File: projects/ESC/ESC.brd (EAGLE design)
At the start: 139.7 x 38.1 mm, 93 parts, among them J1 1755529, J2 1755529, J3 1755529, J4 1755529, U1 STM32F405RGT6, U10 CSD88584Q5DCT, U11 CSD88584Q5DCT, U12 CSD88584Q5DCT, U13 CSD88584Q5DCT, U14 SN74CBTLV3257PWR, U2 CSD88584Q5DCT, U3 CSD88584Q5DCT, U4 CSD88584Q5DCT, U5 CSD88584Q5DCT, U6 CSD88584Q5DCT, U7 CSD88584Q5DCT, U8 CSD88584Q5DCT, U9 CSD88584Q5DCT, Y1 ECS-80-S-4X

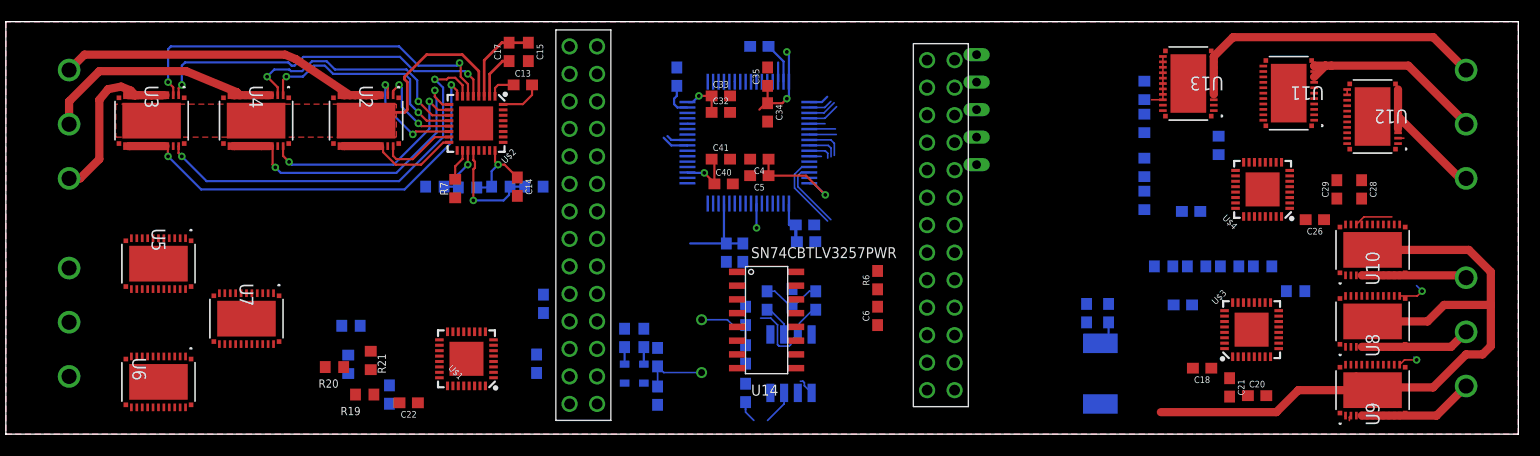
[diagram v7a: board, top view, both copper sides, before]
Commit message: All 4 drive ckts complete
Added and implemented design block across all 4 motors.
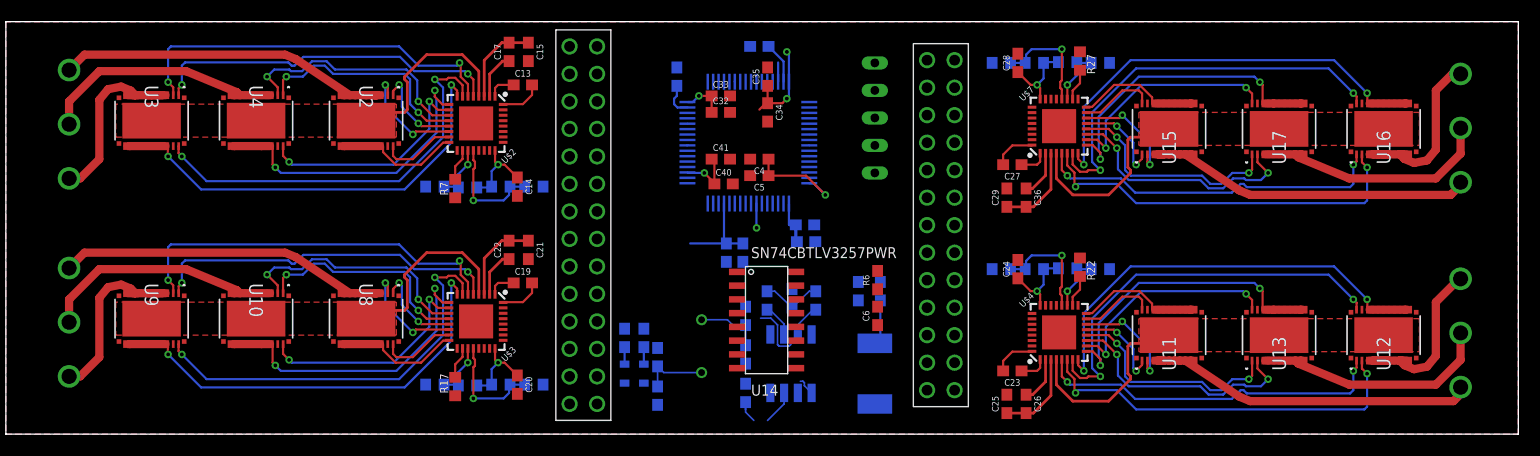
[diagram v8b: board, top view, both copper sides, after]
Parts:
- removed C18: 47nF, SparkFun-Capacitors:0603
- removed R13: 47k, rcl:R0603
- removed R14, R15, R16: (no value), rcl:R0603
- removed U$1: DRV8320H, VESC_SHIT:QFN-32-5X5MM
- removed U5, U6, U7: CSD88584Q5DCT, VESC_SHIT:DMM0022A
- added C36: 1.0uF, SparkFun-Capacitors:0603
- added R30, R31, R32, R33: (no value), rcl:R0603
- added U$7: DRV8320H, VESC_SHIT:QFN-32-5X5MM
- added U15, U16, U17: CSD88584Q5DCT, VESC_SHIT:DMM0022A
- C19, C23, C27: value 1.0uF -> 47nF
- C20, C24, C28: value 0.1uF -> 1.0uF
- C21, C25, C29: value 1.0uF -> 0.1uF
- C22, C26: value 47nF -> 1.0uF
- R17, R22, R27: value (none) -> 47k
- R18, R23: value 47k -> (none)
- moved U9 113.0 mm to (13.5, 10.7), turned to 270 degrees
- moved U10 103.3 mm to (23.1, 10.7), turned to 270 degrees
- moved U8 93.0 mm to (33.3, 10.7), turned to 270 degrees
- moved U$3 71.6 mm to (43.4, 10.4), turned to 180 degrees
- moved C20 68.3 mm to (47.2, 4.57), turned to 270 degrees
- moved R22 68.2 mm to (99.2, 15.4), flipped to the top, turned to 270 degrees
- moved R17 66.4 mm to (41.5, 4.39), flipped to the top, turned to 90 degrees
- moved C21 66.0 mm to (48.3, 17.0)
- moved C19 61.0 mm to (47.8, 14.0), flipped to the top
- moved C23 57.6 mm to (93.0, 5.84), flipped to the top, turned to 180 degrees
- moved C24 45.3 mm to (93.5, 15.2), flipped to the top, turned to 90 degrees
- moved C25 43.8 mm to (92.5, 2.79), flipped to the top
- moved C28 33.8 mm to (93.5, 34.3), turned to 90 degrees
- moved C26 31.6 mm to (94.2, 2.79), turned to 270 degrees
- moved C29 30.5 mm to (92.5, 21.8)
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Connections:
- removed net IDRIVE: R19.1, R20.2, U$1.19
- removed net N$25: C18.2, U$3.32
- removed net N$31: C22.1, U$1.1
- removed net N$40: C29.1, U$4.2
- removed net N$41: C26.1, U$4.1
- removed net N$42: C26.2, U$4.32
- removed net N$43: R24.1, R25.2, U$4.19
- removed net N$44: R23.2, U$4.18
- removed net N$45: R26.1, R27.2, U$4.20
- removed net VDS: R21.1, R22.2, U$1.20
- new net N$11: R17.2, U$3.18
- new net N$12: R22.2, U$4.18
- new net N$13: R27.2, U$7.18
- new net N$21: C22.1, U$3.2
- new net N$22: C19.1, U$3.1
- new net N$29: C23.2, U$4.32
- new net N$33: C36.1, U$7.2
- new net N$36: C27.2, U$7.32
- new net N$37: R30.1, R31.2, U$7.19
- new net N$39: R32.1, R33.2, U$7.20
- net DVDD_2: now also C20.1, R18.2, R20.2, U$3.24; no longer C23.1, R19.2, R21.2, U$1.24
- net DVDD_3: now also C24.1, R23.2, R25.2, U$4.24; no longer C19.1, R14.2, R16.2, U$3.24
- net DVDD_4: now also C28.1, R30.2, R32.2, U$7.24; no longer C27.1, R24.2, R26.2, U$4.24
- net EN_2: now also U$3.22; no longer U$1.22
- net EN_3: now also U$4.22; no longer U$3.22
- net EN_4: now also U$7.22; no longer U$4.22
- net FAULT_2: now also U$3.17; no longer U$1.17
- net FAULT_3: now also U$4.17; no longer U$3.17
- net FAULT_4: now also U$7.17; no longer U$4.17
- net GHA_2: now also U$3.5, U9.1; no longer U$1.5, U6.1
- net GHA_3: now also U$4.5, U12.1; no longer U$3.5, U9.1
- net GHA_4: now also U$7.5, U16.1; no longer U$4.5, U12.1
- net GHB_2: now also U$3.12, U10.1; no longer U$1.12, U5.1
- net GHB_3: now also U$4.12, U13.1; no longer U$3.12, U8.1
- net GHB_4: now also U$7.12, U17.1; no longer U$4.12, U11.1
- net GHC_2: now also U$3.13, U8.1; no longer U$1.13, U7.1
- net GHC_3: now also U$4.13, U11.1; no longer U$3.13, U10.1
- net GHC_4: now also U$7.13, U15.1; no longer U$4.13, U13.1
- net GLA_2: now also U$3.7, U9.22; no longer U$1.7, U6.22
- net GLA_3: now also U$4.7, U12.22; no longer U$3.7, U9.22
- net GLA_4: now also U$7.7, U16.22; no longer U$4.7, U12.22
- net GLB_2: now also U$3.10, U10.22; no longer U$1.10, U5.22
- net GLB_3: now also U$4.10, U13.22; no longer U$3.10, U8.22
- net GLB_4: now also U$7.10, U17.22; no longer U$4.10, U11.22
- net GLC_2: now also U$3.15, U8.22; no longer U$1.15, U7.22
- net GLC_3: now also U$4.15, U11.22; no longer U$3.15, U10.22
- net GLC_4: now also U$7.15, U15.22; no longer U$4.15, U13.22
- net GND: now also C21.2, C25.2, C29.2, R19.1, R21.1, R24.1, R26.1, R31.1, R33.1, U$7.23, U$7.31, U$7.EP; no longer C19.2, C23.2, C27.2, R13.1, R15.1, R18.1, R20.1, R23.1, R25.1, U$1.23, U$1.31, U$1.EP
- net INHA_2: now also U$3.25; no longer U$1.25
- net INHA_3: now also U$4.25; no longer U$3.25
- net INHA_4: now also U$7.25; no longer U$4.25
- net INHB_2: now also U$3.27; no longer U$1.27
- net INHB_3: now also U$4.27; no longer U$3.27
- net INHB_4: now also U$7.27; no longer U$4.27
- net INHC_2: now also U$3.29; no longer U$1.29
- net INHC_3: now also U$4.29; no longer U$3.29
- net INHC_4: now also U$7.29; no longer U$4.29
- net INL_2: now also U$3.26, U$3.28, U$3.30; no longer U$1.26, U$1.28, U$1.30
- net INL_3: now also U$4.26, U$4.28, U$4.30; no longer U$3.26, U$3.28, U$3.30
- net INL_4: now also U$7.26, U$7.28, U$7.30; no longer U$4.26, U$4.28, U$4.30
- net N$23: now also C19.2, U$3.32; no longer C21.1, U$3.2
- net N$24: now also R18.1, R19.2, U$3.19; no longer C18.1, U$3.1
- net N$26: now also R20.1, R21.2, U$3.20; no longer R14.1, R15.2, U$3.19
- net N$27: now also C26.1, U$4.2; no longer R13.2, U$3.18
- net N$28: now also C23.1, U$4.1; no longer R16.1, R17.2, U$3.20
- net N$30: now also R23.1, R24.2, U$4.19; no longer C25.1, U$1.2
- net N$32: now also R25.1, R26.2, U$4.20; no longer C22.2, U$1.32
- net N$35: now also C27.1, U$7.1; no longer R18.2, U$1.18
- net PHASE_A2: now also U9.10, U9.11, U9.3, U9.4, U9.5, U9.6, U9.7, U9.8, U9.9; no longer U6.10, U6.11, U6.3, U6.4, U6.5, U6.6, U6.7, U6.8, U6.9
- net PHASE_A3: now also U12.10, U12.11, U12.3, U12.4, U12.5, U12.6, U12.7, U12.8, U12.9; no longer U9.10, U9.11, U9.3, U9.4, U9.5, U9.6, U9.7, U9.8, U9.9
- net PHASE_A4: now also U16.10, U16.11, U16.3, U16.4, U16.5, U16.6, U16.7, U16.8, U16.9; no longer U12.10, U12.11, U12.3, U12.4, U12.5, U12.6, U12.7, U12.8, U12.9
- net PHASE_B2: now also U10.10, U10.11, U10.3, U10.4, U10.5, U10.6, U10.7, U10.8, U10.9; no longer U5.10, U5.11, U5.3, U5.4, U5.5, U5.6, U5.7, U5.8, U5.9
- net PHASE_B3: now also U13.10, U13.11, U13.3, U13.4, U13.5, U13.6, U13.7, U13.8, U13.9; no longer U8.10, U8.11, U8.3, U8.4, U8.5, U8.6, U8.7, U8.8, U8.9
- net PHASE_B4: now also U17.10, U17.11, U17.3, U17.4, U17.5, U17.6, U17.7, U17.8, U17.9; no longer U11.10, U11.11, U11.3, U11.4, U11.5, U11.6, U11.7, U11.8, U11.9
- net PHASE_C2: now also U8.10, U8.11, U8.3, U8.4, U8.5, U8.6, U8.7, U8.8, U8.9; no longer U7.10, U7.11, U7.3, U7.4, U7.5, U7.6, U7.7, U7.8, U7.9
- net PHASE_C3: now also U11.10, U11.11, U11.3, U11.4, U11.5, U11.6, U11.7, U11.8, U11.9; no longer U10.10, U10.11, U10.3, U10.4, U10.5, U10.6, U10.7, U10.8, U10.9
- net PHASE_C4: now also U15.10, U15.11, U15.3, U15.4, U15.5, U15.6, U15.7, U15.8, U15.9; no longer U13.10, U13.11, U13.3, U13.4, U13.5, U13.6, U13.7, U13.8, U13.9
- net SHA_2: now also U$3.6, U9.2; no longer U$1.6, U6.2
- net SHA_3: now also U$4.6, U12.2; no longer U$3.6, U9.2
- net SHA_4: now also U$7.6, U16.2; no longer U$4.6, U12.2
- net SHB_2: now also U$3.11, U10.2; no longer U$1.11, U5.2
- net SHB_3: now also U$4.11, U13.2; no longer U$3.11, U8.2
- net SHB_4: now also U$7.11, U17.2; no longer U$4.11, U11.2
- net SHC_2: now also U$3.14, U8.2; no longer U$1.14, U7.2
- net SHC_3: now also U$4.14, U11.2; no longer U$3.14, U10.2
- net SHC_4: now also U$7.14, U15.2; no longer U$4.14, U13.2
- net SLA_2: now also U$3.8, U9.12, U9.13, U9.14, U9.15, U9.16, U9.17, U9.18, U9.19, U9.20; no longer U$1.8, U6.12, U6.13, U6.14, U6.15, U6.16, U6.17, U6.18, U6.19, U6.20
- net SLA_3: now also U$4.8, U12.12, U12.13, U12.14, U12.15, U12.16, U12.17, U12.18, U12.19, U12.20; no longer U$3.8, U9.12, U9.13, U9.14, U9.15, U9.16, U9.17, U9.18, U9.19, U9.20
- net SLA_4: now also U$7.8, U16.12, U16.13, U16.14, U16.15, U16.16, U16.17, U16.18, U16.19, U16.20; no longer U$4.8, U12.12, U12.13, U12.14, U12.15, U12.16, U12.17, U12.18, U12.19, U12.20
- net SLB_2: now also U$3.9, U10.12, U10.13, U10.14, U10.15, U10.16, U10.17, U10.18, U10.19, U10.20; no longer U$1.9, U5.12, U5.13, U5.14, U5.15, U5.16, U5.17, U5.18, U5.19, U5.20
- net SLB_3: now also U$4.9, U13.12, U13.13, U13.14, U13.15, U13.16, U13.17, U13.18, U13.19, U13.20; no longer U$3.9, U8.12, U8.13, U8.14, U8.15, U8.16, U8.17, U8.18, U8.19, U8.20
- net SLB_4: now also U$7.9, U17.12, U17.13, U17.14, U17.15, U17.16, U17.17, U17.18, U17.19, U17.20; no longer U$4.9, U11.12, U11.13, U11.14, U11.15, U11.16, U11.17, U11.18, U11.19, U11.20
- net SLC_2: now also U$3.16, U8.12, U8.13, U8.14, U8.15, U8.16, U8.17, U8.18, U8.19, U8.20; no longer U$1.16, U7.12, U7.13, U7.14, U7.15, U7.16, U7.17, U7.18, U7.19, U7.20
- net SLC_3: now also U$4.16, U11.12, U11.13, U11.14, U11.15, U11.16, U11.17, U11.18, U11.19, U11.20; no longer U$3.16, U10.12, U10.13, U10.14, U10.15, U10.16, U10.17, U10.18, U10.19, U10.20
- net SLC_4: now also U$7.16, U15.12, U15.13, U15.14, U15.15, U15.16, U15.17, U15.18, U15.19, U15.20; no longer U$4.16, U13.12, U13.13, U13.14, U13.15, U13.16, U13.17, U13.18, U13.19, U13.20
- net VM_2: now also C21.1, C22.2, U$3.3, U$3.4, U10.27, U8.27, U9.27; no longer C24.1, C25.2, U$1.3, U$1.4, U5.27, U6.27, U7.27
- net VM_3: now also C25.1, C26.2, U$4.3, U$4.4, U11.27, U12.27, U13.27; no longer C20.1, C21.2, U$3.3, U$3.4, U10.27, U8.27, U9.27
- net VM_4: now also C29.1, C36.2, U$7.3, U$7.4, U15.27, U16.27, U17.27; no longer C28.1, C29.2, U$4.3, U$4.4, U11.27, U12.27, U13.27
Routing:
- net SLA_2: track 0.00 -> 40.3 mm, vias 0 -> 2
- net VM_3: track 66.3 -> 26.1 mm
- net SLA_4: track 0.50 -> 40.3 mm, vias 0 -> 2
- net SLA_3: track 2.11 -> 40.3 mm, vias 1 -> 2
- net GLA_3: track 0.00 -> 37.4 mm, vias 0 -> 2
- net GLA_4: track 0.00 -> 37.4 mm, vias 0 -> 2
- net GLA_2: track 0.00 -> 37.4 mm, vias 0 -> 2
- net SHA_2: track 0.00 -> 35.7 mm, vias 0 -> 2
- net SHA_3: track 0.51 -> 35.7 mm, vias 0 -> 2
- net SHA_4: track 0.54 -> 35.7 mm, vias 0 -> 2
- net GHA_4: track 0.00 -> 32.8 mm, vias 0 -> 2
- net GHA_2: track 0.00 -> 32.8 mm, vias 0 -> 2
- net GHA_3: track 0.10 -> 32.8 mm, vias 0 -> 2
- net PHASE_C2: track 0.00 -> 31.8 mm
- net SLB_2: track 0.00 -> 29.3 mm, vias 0 -> 2
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- added copper zone on layer 1, net VM_2
- added copper zone on layer 1, net VM_3
- added copper zone on layer 1, net VM_4
